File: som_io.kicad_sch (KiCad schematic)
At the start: 32 parts, among them J1 Hermaphroditic_Molex_203456-0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, J20 Tag-Connect_TC2050-IDC-NL_2x5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, Q28 PJE138K, U1 NTS0102_XSON, U2 NTS0102_XSON, U3 NTS0102_XSON, U39 NTS0102_XSON, U4 NTS0102_XSON, U5 NTS0102_XSON, U59 TXU0304BQAR

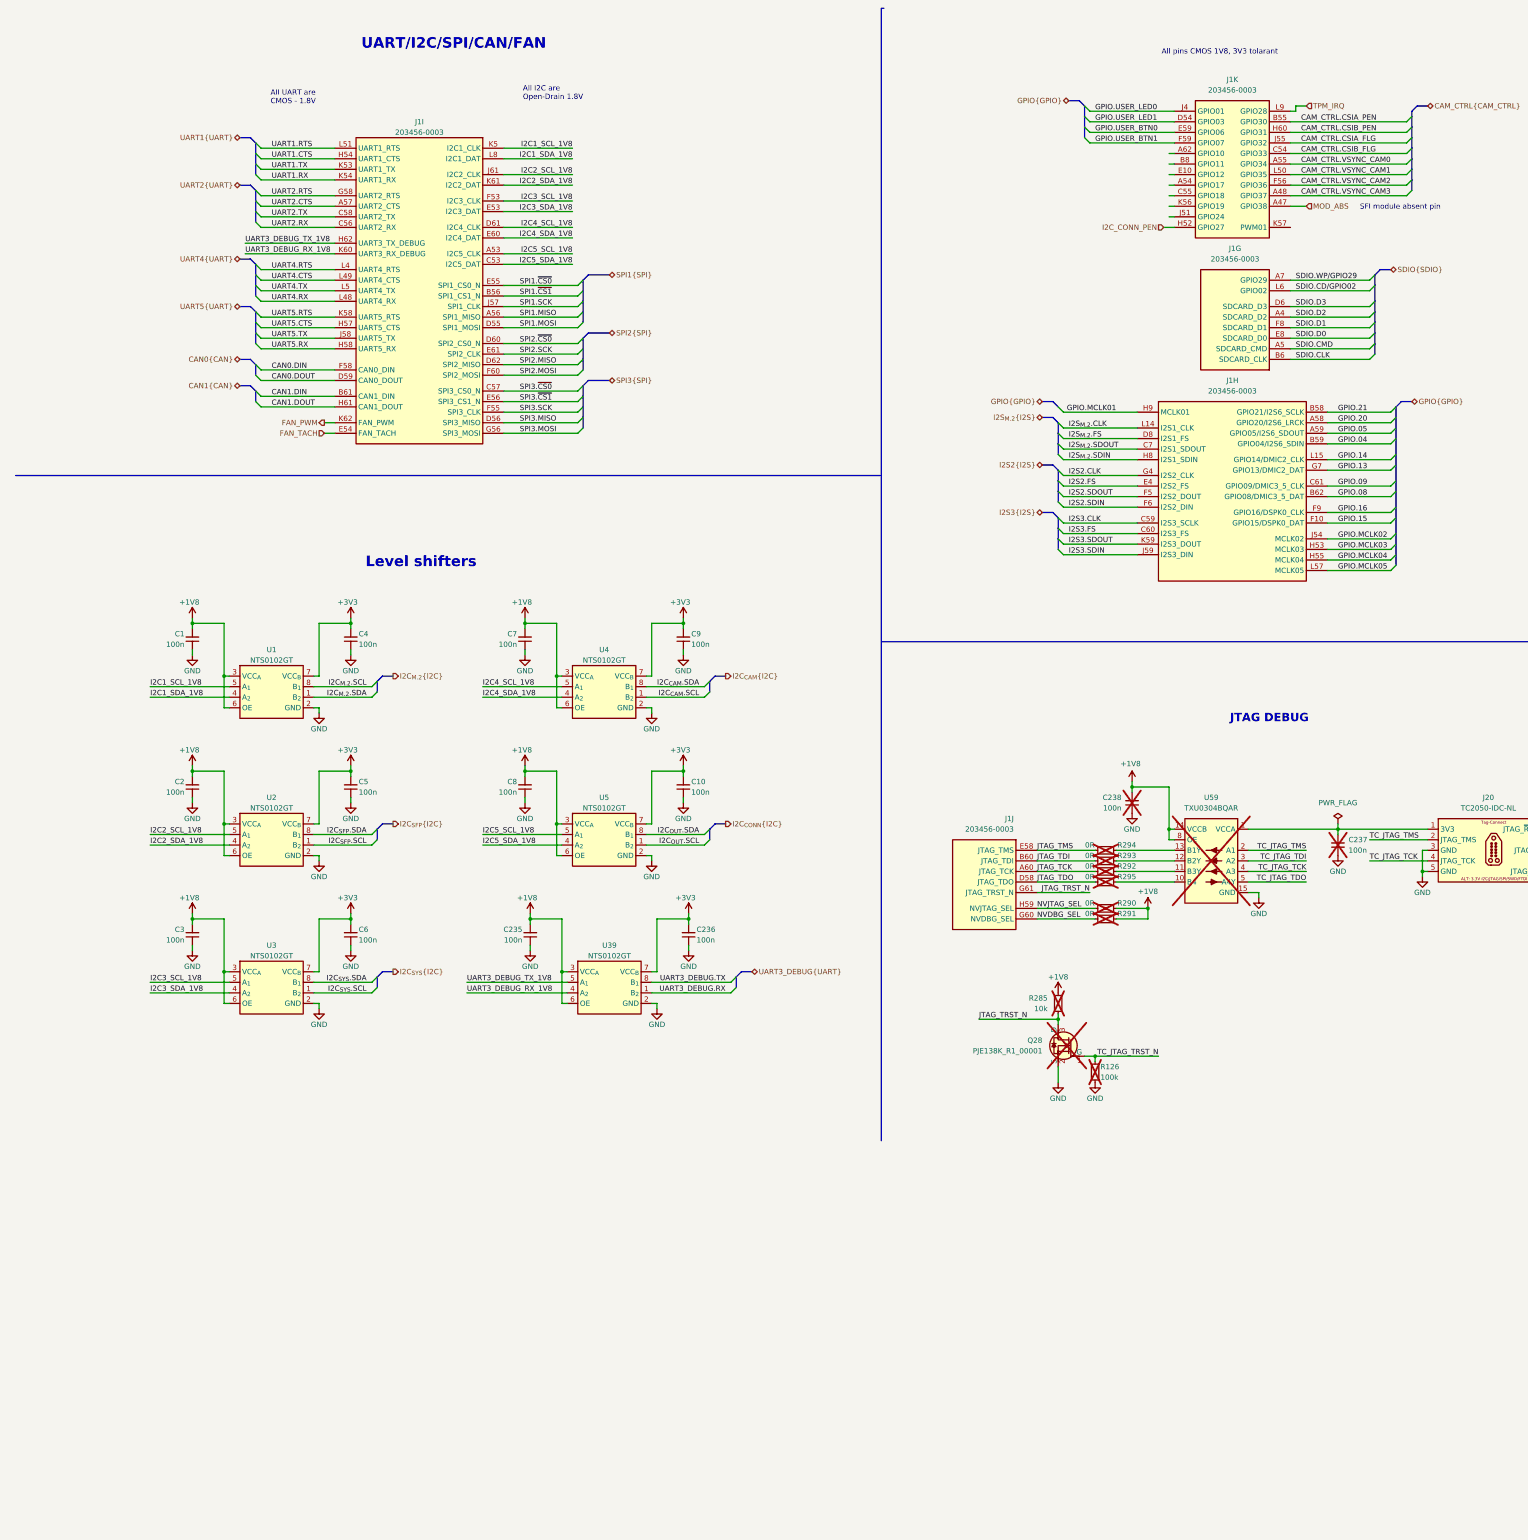
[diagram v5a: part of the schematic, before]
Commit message: [#82837] Map interfaces from AGX to Thor on SoM schematic and add level shifters for 1V8 interfaces
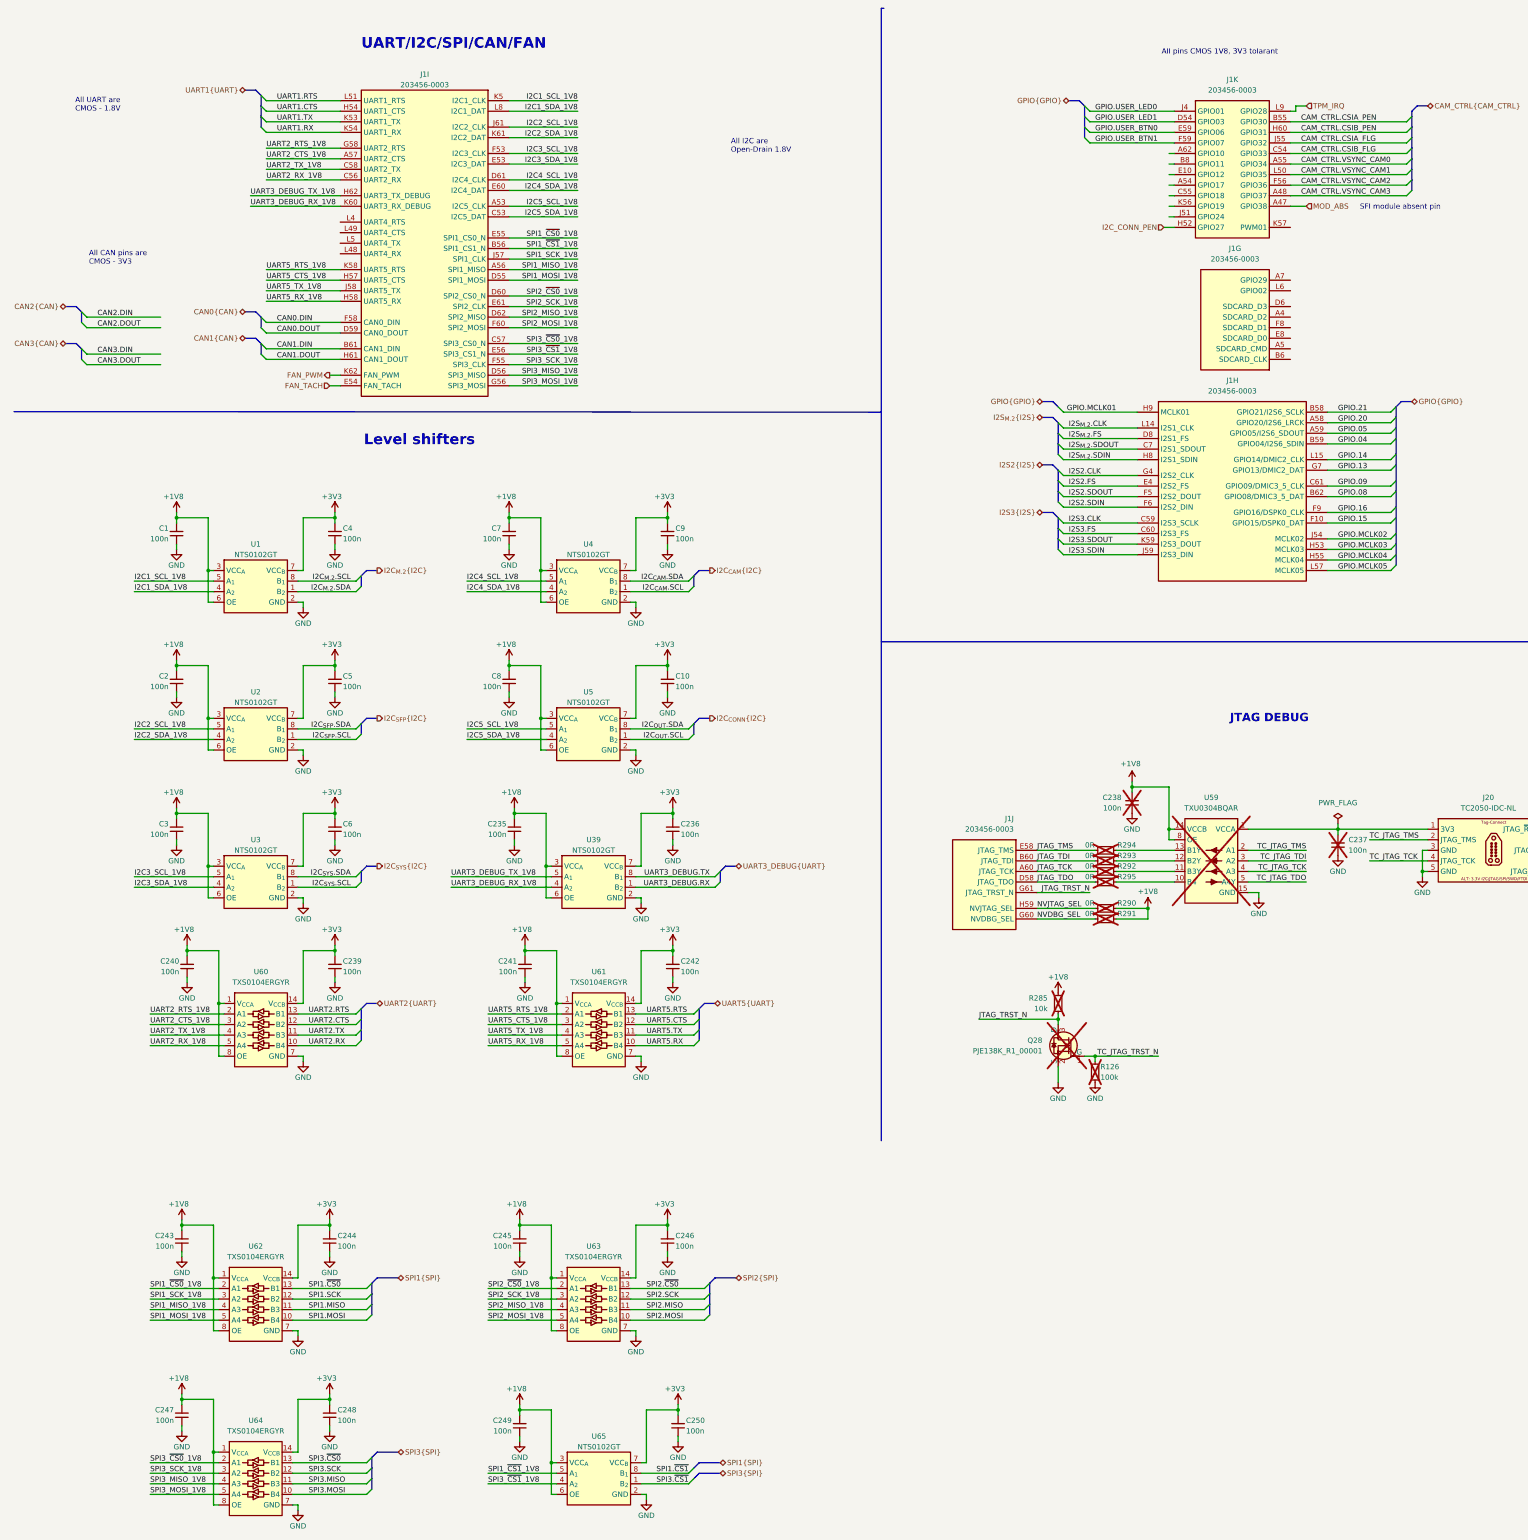
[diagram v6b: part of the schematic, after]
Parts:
- added C239, C240, C241, C242, C243, C244, C245, C246, C247, C248, C249, C250: C_100n_0402, antmicro-footprints:C_0402_1005Metric, symbol antmicroCapacitors0402:C_100n_0402
- added U60, U61, U62, U63, U64: TXS0104E_VQFN, antmicro-footprints:VQFN-14-1EP_3.65x3.65mm_P0.5mm_Layout5x2, symbol antmicroLogicTranslatorsLevelShifters:TXS0104E_VQFN
- added U65: NTS0102_XSON, antmicro-footprints:XSON-8_1x1.95mm_P0.5mm, symbol antmicroLogicTranslatorsLevelShifters:NTS0102_XSON
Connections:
- net +1V8: now also C240.2, C241.2, C243.2, C245.2, C247.2, C249.2, U60.1 (V_{CCA}), U60.8 (OE), U61.1 (V_{CCA}), U61.8 (OE), U62.1 (V_{CCA}), U62.8 (OE), U63.1 (V_{CCA}), U63.8 (OE), U64.1 (V_{CCA}), U64.8 (OE), U65.3 (VCC_{A}), U65.6 (OE)
- net +3V3: now also C239.2, C242.2, C244.2, C246.2, C248.2, C250.2, U60.14 (V_{CCB}), U61.14 (V_{CCB}), U62.14 (V_{CCB}), U63.14 (V_{CCB}), U64.14 (V_{CCB}), U65.7 (VCC_{B})
- net GND: now also C239.1, C240.1, C241.1, C242.1, C243.1, C244.1, C245.1, C246.1, C247.1, C248.1, C249.1, C250.1, U60.15 (GND), U60.7 (GND), U61.15 (GND), U61.7 (GND), U62.15 (GND), U62.7 (GND), U63.15 (GND), U63.7 (GND), U64.15 (GND), U64.7 (GND), U65.2 (GND)
- net SPI1.MISO: now also U62.11 (B3); no longer J1.A56 (SPI1_MISO)
- net SPI1.MOSI: now also U62.10 (B4); no longer J1.D55 (SPI1_MOSI)
- net SPI1.SCK: now also U62.12 (B2); no longer J1.J57 (SPI1_CLK)
- net SPI1.~{CS0}: now also U62.13 (B1); no longer J1.E55 (SPI1_CS0_N)
- net SPI1.~{CS1}: now also U65.8 (B_{1}); no longer J1.B56 (SPI1_CS1_N)
- net SPI2.MISO: now also U63.11 (B3); no longer J1.D62 (SPI2_MISO)
- net SPI2.MOSI: now also U63.10 (B4); no longer J1.F60 (SPI2_MOSI)
- net SPI2.SCK: now also U63.12 (B2); no longer J1.E61 (SPI2_CLK)
- net SPI2.~{CS0}: now also U63.13 (B1); no longer J1.D60 (SPI2_CS0_N)
- net SPI3.MISO: now also U64.11 (B3); no longer J1.D56 (SPI3_MISO)
- net SPI3.MOSI: now also U64.10 (B4); no longer J1.G56 (SPI3_MOSI)
- net SPI3.SCK: now also U64.12 (B2); no longer J1.F55 (SPI3_CLK)
- net SPI3.~{CS0}: now also U64.13 (B1); no longer J1.C57 (SPI3_CS0_N)
- net SPI3.~{CS1}: now also U65.1 (B_{2}); no longer J1.E56 (SPI3_CS1_N)
- net UART2.CTS: now also U60.12 (B2); no longer J1.A57 (UART2_CTS)
- net UART2.RTS: now also U60.13 (B1); no longer J1.G58 (UART2_RTS)
- net UART2.RX: now also U60.10 (B4); no longer J1.C56 (UART2_RX)
- net UART2.TX: now also U60.11 (B3); no longer J1.C58 (UART2_TX)
- net UART5.CTS: now also U61.12 (B2); no longer J1.H57 (UART5_CTS)
- net UART5.RTS: now also U61.13 (B1); no longer J1.K58 (UART5_RTS)
- net UART5.RX: now also U61.10 (B4); no longer J1.H58 (UART5_RX)
- net UART5.TX: now also U61.11 (B3); no longer J1.J58 (UART5_TX)
- net SDIO.CD/GPIO02: no longer names the net of J1.L6 (GPIO02)
- net SDIO.CLK: no longer names the net of J1.B6 (SDCARD_CLK)
- net SDIO.CMD: no longer names the net of J1.A5 (SDCARD_CMD)
- net SDIO.D0: no longer names the net of J1.E8 (SDCARD_D0)
- net SDIO.D1: no longer names the net of J1.F8 (SDCARD_D1)
- net SDIO.D2: no longer names the net of J1.A4 (SDCARD_D2)
- net SDIO.D3: no longer names the net of J1.D6 (SDCARD_D3)
- net SDIO.WP/GPIO29: no longer names the net of J1.A7 (GPIO29)
- net UART4.CTS: no longer names the net of J1.L49 (UART4_CTS)
- net UART4.RTS: no longer names the net of J1.L4 (UART4_RTS)
- net UART4.RX: no longer names the net of J1.L48 (UART4_RX)
- net UART4.TX: no longer names the net of J1.L5 (UART4_TX)
- new net SPI1_MISO_1V8: J1.A56 (SPI1_MISO), U62.4 (A3)
- new net SPI1_MOSI_1V8: J1.D55 (SPI1_MOSI), U62.5 (A4)
- new net SPI1_SCK_1V8: J1.J57 (SPI1_CLK), U62.3 (A2)
- new net SPI1_~{CS0}_1V8: J1.E55 (SPI1_CS0_N), U62.2 (A1)
- new net SPI1_~{CS1}_1V8: J1.B56 (SPI1_CS1_N), U65.5 (A_{1})
- new net SPI2_MISO_1V8: J1.D62 (SPI2_MISO), U63.4 (A3)
- new net SPI2_MOSI_1V8: J1.F60 (SPI2_MOSI), U63.5 (A4)
- new net SPI2_SCK_1V8: J1.E61 (SPI2_CLK), U63.3 (A2)
- new net SPI2_~{CS0}_1V8: J1.D60 (SPI2_CS0_N), U63.2 (A1)
- new net SPI3_MISO_1V8: J1.D56 (SPI3_MISO), U64.4 (A3)
- new net SPI3_MOSI_1V8: J1.G56 (SPI3_MOSI), U64.5 (A4)
- new net SPI3_SCK_1V8: J1.F55 (SPI3_CLK), U64.3 (A2)
- new net SPI3_~{CS0}_1V8: J1.C57 (SPI3_CS0_N), U64.2 (A1)
- new net SPI3_~{CS1}_1V8: J1.E56 (SPI3_CS1_N), U65.4 (A_{2})
- new net UART2_CTS_1V8: J1.A57 (UART2_CTS), U60.3 (A2)
- new net UART2_RTS_1V8: J1.G58 (UART2_RTS), U60.2 (A1)
- new net UART2_RX_1V8: J1.C56 (UART2_RX), U60.5 (A4)
- new net UART2_TX_1V8: J1.C58 (UART2_TX), U60.4 (A3)
- new net UART5_CTS_1V8: J1.H57 (UART5_CTS), U61.3 (A2)
- new net UART5_RTS_1V8: J1.K58 (UART5_RTS), U61.2 (A1)
- new net UART5_RX_1V8: J1.H58 (UART5_RX), U61.5 (A4)
- new net UART5_TX_1V8: J1.J58 (UART5_TX), U61.4 (A3)
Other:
- note added: "All CAN pins are CMOS - 3V3"
- moved on the sheet: C1, C10, C2, C235, C236, C3, C4, C5, C6, C7, C8, C9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

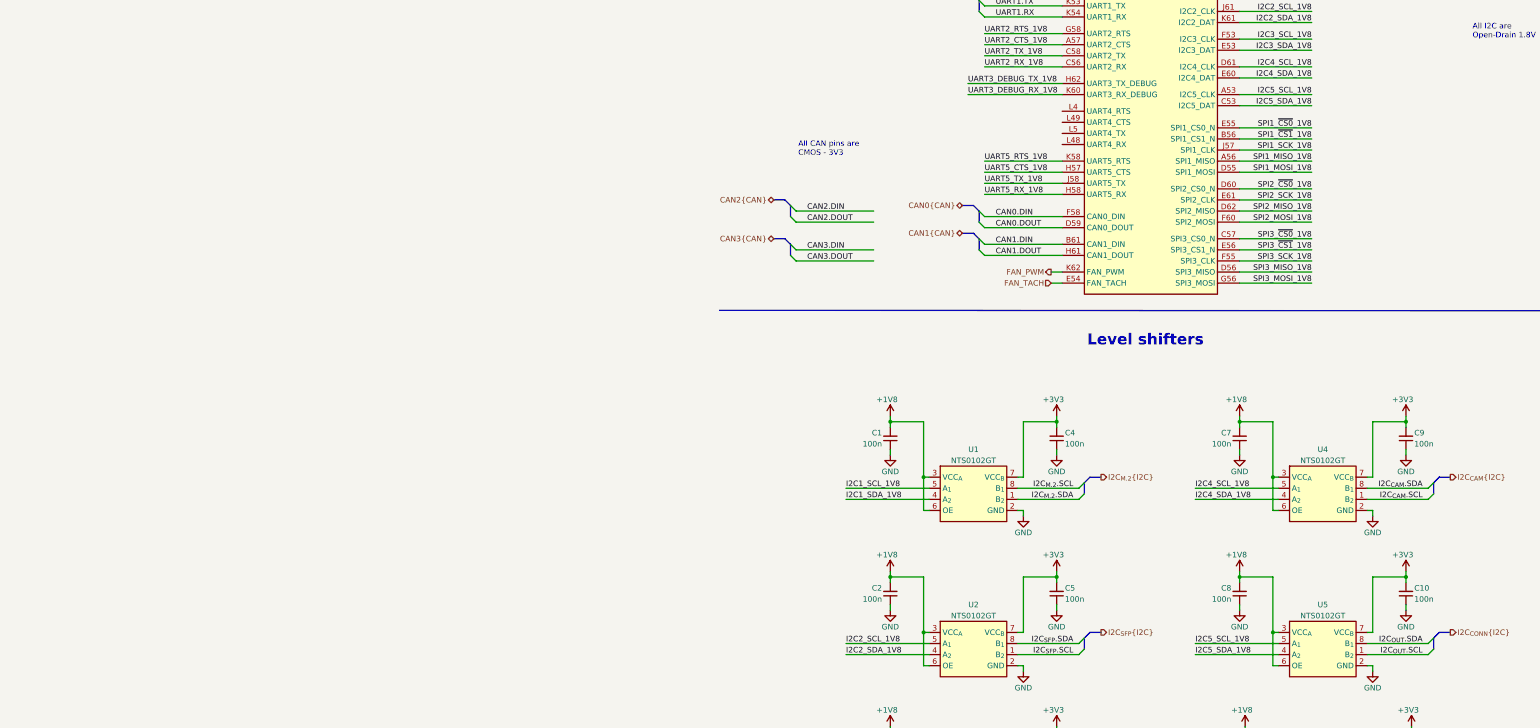
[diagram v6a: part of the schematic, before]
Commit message: [#82837] Map interfaces on expansion connector
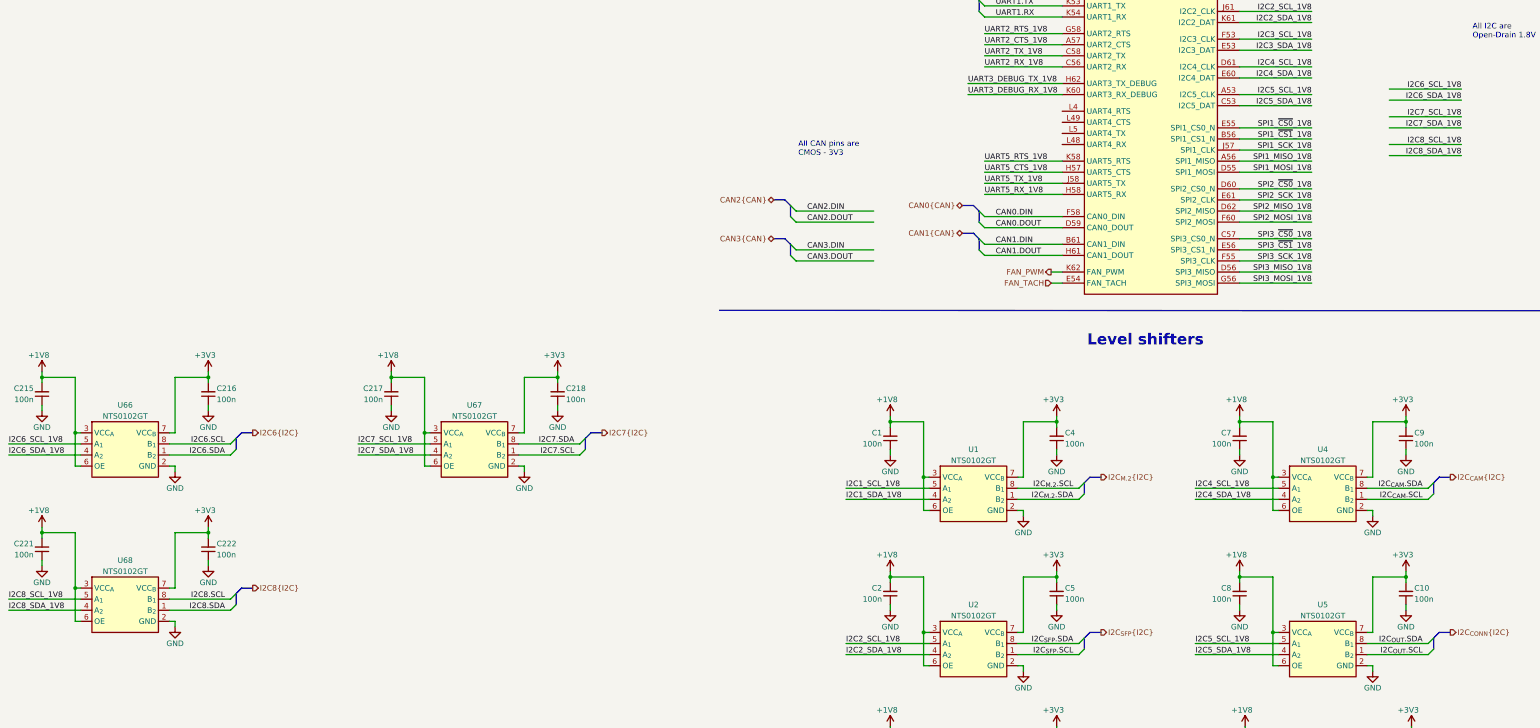
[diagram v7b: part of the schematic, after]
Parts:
- added C215, C216, C217, C218, C221, C222: C_100n_0402, antmicro-footprints:C_0402_1005Metric, symbol antmicroCapacitors0402:C_100n_0402
- added U66, U67, U68: NTS0102_XSON, antmicro-footprints:XSON-8_1x1.95mm_P0.5mm, symbol antmicroLogicTranslatorsLevelShifters:NTS0102_XSON
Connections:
- net +1V8: now also C215.2, C217.2, C221.2, U66.3 (VCC_{A}), U66.6 (OE), U67.3 (VCC_{A}), U67.6 (OE), U68.3 (VCC_{A}), U68.6 (OE)
- net +3V3: now also C216.2, C218.2, C222.2, U66.7 (VCC_{B}), U67.7 (VCC_{B}), U68.7 (VCC_{B})
- net GND: now also C215.1, C216.1, C217.1, C218.1, C221.1, C222.1, U66.2 (GND), U67.2 (GND), U68.2 (GND)
- new net I2C6.SCL: U66.8 (B_{1})
- new net I2C6.SDA: U66.1 (B_{2})
- new net I2C6_SCL_1V8: U66.5 (A_{1})
- new net I2C6_SDA_1V8: U66.4 (A_{2})
- new net I2C7.SCL: U67.1 (B_{2})
- new net I2C7.SDA: U67.8 (B_{1})
- new net I2C7_SCL_1V8: U67.5 (A_{1})
- new net I2C7_SDA_1V8: U67.4 (A_{2})
- new net I2C8.SCL: U68.8 (B_{1})
- new net I2C8.SDA: U68.1 (B_{2})
- new net I2C8_SCL_1V8: U68.5 (A_{1})
- new net I2C8_SDA_1V8: U68.4 (A_{2})
